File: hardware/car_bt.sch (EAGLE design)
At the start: 51 parts, among them IC2 MIC5209, U1 ATMEGA328P_TQFP, U2 ADP1710-2.5V, Y1 11.0592MHz

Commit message: selected components
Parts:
- added C21: 22uF, resistor:C-EUC1206
- added C22: 22uF, SparkFun-Passives:CAP_POL3528
- C1, C2, C3: value 47uF -> 22uF; device resistor:C-EUC1210 -> resistor:C-EUC1206
- C11, C12, C13, C15, C16, C17, C18, C19, C20, C7, C8: device resistor:C-EUC1210 -> resistor:C-EUC0805
- C4, C5: device resistor:C-EUC0603 -> resistor:C-EUC0805
- L1: value 12uH -> 10uH; device resistor:L-EUL3225P -> resistor:L-EUL3216C
- R1, R11, R12, R13, R14, R2, R21, R3, R4, R5, R6, R7, R8: device rcl:R-EU_R0603 -> rcl:R-EU_R0805
- R10: value 330 -> 360; device rcl:R-EU_R0603 -> rcl:R-EU_R0805
- R9: value 470 -> 360; device rcl:R-EU_R0603 -> rcl:R-EU_R0805
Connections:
- net +5V: now also C2.1, C22.+; no longer C1.1
- net DGND: now also C1.2, C21.2; no longer C2.2
- net GND: now also C2.2, C22.-; no longer C1.2
- net V+: now also C21.1
- net VCC-ISO: now also C1.1; no longer C2.1
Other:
- moved on the sheet: C1, C2

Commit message: v 1.0 of hardware completed
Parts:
- JP2: value (none) -> CAR_IN; device pinhead:PINHD-1X8 -> pinhead:PINHD-1X8/90
- Q2: value (none) -> 2N3904
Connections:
- net V+: no longer R5.1
- net VCC-ISO: now also R5.1
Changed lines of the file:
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@@
 <part name="P+1" library="supply1" deviceset="+5V" device=""/>
 <part name="P+2" library="supply1" deviceset="+5V" device=""/>
-<part name="JP2" library="pinhead" deviceset="PINHD-1X8" device=""/>
+<part name="JP2" library="pinhead" deviceset="PINHD-1X8" device="/90" value="CAR_IN"/>
 <part name="R2" library="rcl" deviceset="R-EU_" device="R0805" value="470"/>
 <part name="R3" library="rcl" deviceset="R-EU_" device="R0805" value="220"/>
@@
 <part name="JP4" library="SparkFun-Connectors" deviceset="M02" device="POLAR_LOCK" value="MIC"/>
 <part name="R5" library="rcl" deviceset="R-EU_" device="R0805" value="220"/>
-<part name="P+8" library="supply1" deviceset="V+" device=""/>
 <part name="SUPPLY3" library="supply2" deviceset="DGND" device=""/>
 <part name="JP5" library="SparkFun-Connectors" deviceset="M01" device="PTH_LONGPAD" value="REMOTE"/>
@@
 <part name="SUPPLY6" library="SparkFun-Aesthetics" deviceset="VCCIO" device=""/>
 <part name="SUPPLY9" library="supply2" deviceset="DGND" device=""/>
-<part name="Q2" library="SparkFun-DiscreteSemi" deviceset="TRANSISTOR_NPN" device="BC547"/>
+<part name="Q2" library="SparkFun-DiscreteSemi" deviceset="TRANSISTOR_NPN" device="BC547" value="2N3904"/>
 <part name="R12" library="rcl" deviceset="R-EU_" device="R0805" value="470"/>
 <part name="SUPPLY10" library="supply2" deviceset="DGND" device=""/>
@@
 <part name="P+18" library="supply1" deviceset="+5V" device=""/>
 <part name="GND15" library="supply1" deviceset="GND" device=""/>
+<part name="U$4" library="SparkFun-Aesthetics" deviceset="VCC-ISO" device=""/>
 </parts>
 <sheets>
@@
 <instance part="JP4" gate="G$1" x="-111.76" y="-96.52"/>
 <instance part="R5" gate="G$1" x="22.86" y="58.42" rot="R270"/>
-<instance part="P+8" gate="1" x="22.86" y="66.04"/>
 <instance part="SUPPLY3" gate="G$1" x="22.86" y="50.8"/>
 <instance part="JP5" gate="G$1" x="30.48" y="2.54" rot="R180"/>
@@
 <instance part="P+18" gate="1" x="-76.2" y="88.9"/>
 <instance part="GND15" gate="1" x="-76.2" y="73.66"/>
+<instance part="U$4" gate="G$1" x="22.86" y="63.5"/>
 </instances>
 <busses>
@@
 <pinref part="C10" gate="G$1" pin="+"/>
 <junction x="-12.7" y="60.96"/>
-</segment>
-<segment>
-<pinref part="R5" gate="G$1" pin="1"/>
-<pinref part="P+8" gate="1" pin="V+"/>
 </segment>
 <segment>
@@
 <net name="N$12" class="1">
 <segment>
-<wire x1="-22.86" y1="-109.22" x2="-25.4" y2="-109.22" width="0.1524" layer="91"/>
-<pinref part="U$1" gate="G$1" pin="RST"/>
-<wire x1="-25.4" y1="-109.22" x2="-30.48" y2="-109.22" width="0.1524" layer="91"/>
-<wire x1="-22.86" y1="-109.22" x2="-25.4" y2="-109.22" width="0.1524" layer="91"/>
 <pinref part="OK4" gate="A" pin="COL"/>
 <wire x1="27.94" y1="-111.76" x2="10.16" y2="-111.76" width="0.1524" layer="91"/>
-<wire x1="10.16" y1="-111.76" x2="-22.86" y2="-111.76" width="0.1524" layer="91"/>
-<wire x1="-22.86" y1="-111.76" x2="-22.86" y2="-109.22" width="0.1524" layer="91"/>
+<wire x1="10.16" y1="-111.76" x2="-25.4" y2="-111.76" width="0.1524" layer="91"/>
 <pinref part="R21" gate="G$1" pin="1"/>
 <junction x="10.16" y="-111.76"/>
 <pinref part="C13" gate="G$1" pin="1"/>
-<wire x1="-22.86" y1="-109.22" x2="-25.4" y2="-109.22" width="0.1524" layer="91"/>
+<wire x1="-25.4" y1="-111.76" x2="-25.4" y2="-109.22" width="0.1524" layer="91"/>
+<pinref part="U$1" gate="G$1" pin="RST"/>
+<wire x1="-25.4" y1="-109.22" x2="-30.48" y2="-109.22" width="0.1524" layer="91"/>
 </segment>
 </net>
@@
 <wire x1="5.08" y1="-58.42" x2="5.08" y2="-60.96" width="0.1524" layer="91"/>
 </segment>
-</net>
+<segment>
+<pinref part="R5" gate="G$1" pin="1"/>
+<pinref part="U$4" gate="G$1" pin="VCC-ISO"/>
+</segment>
+</net>

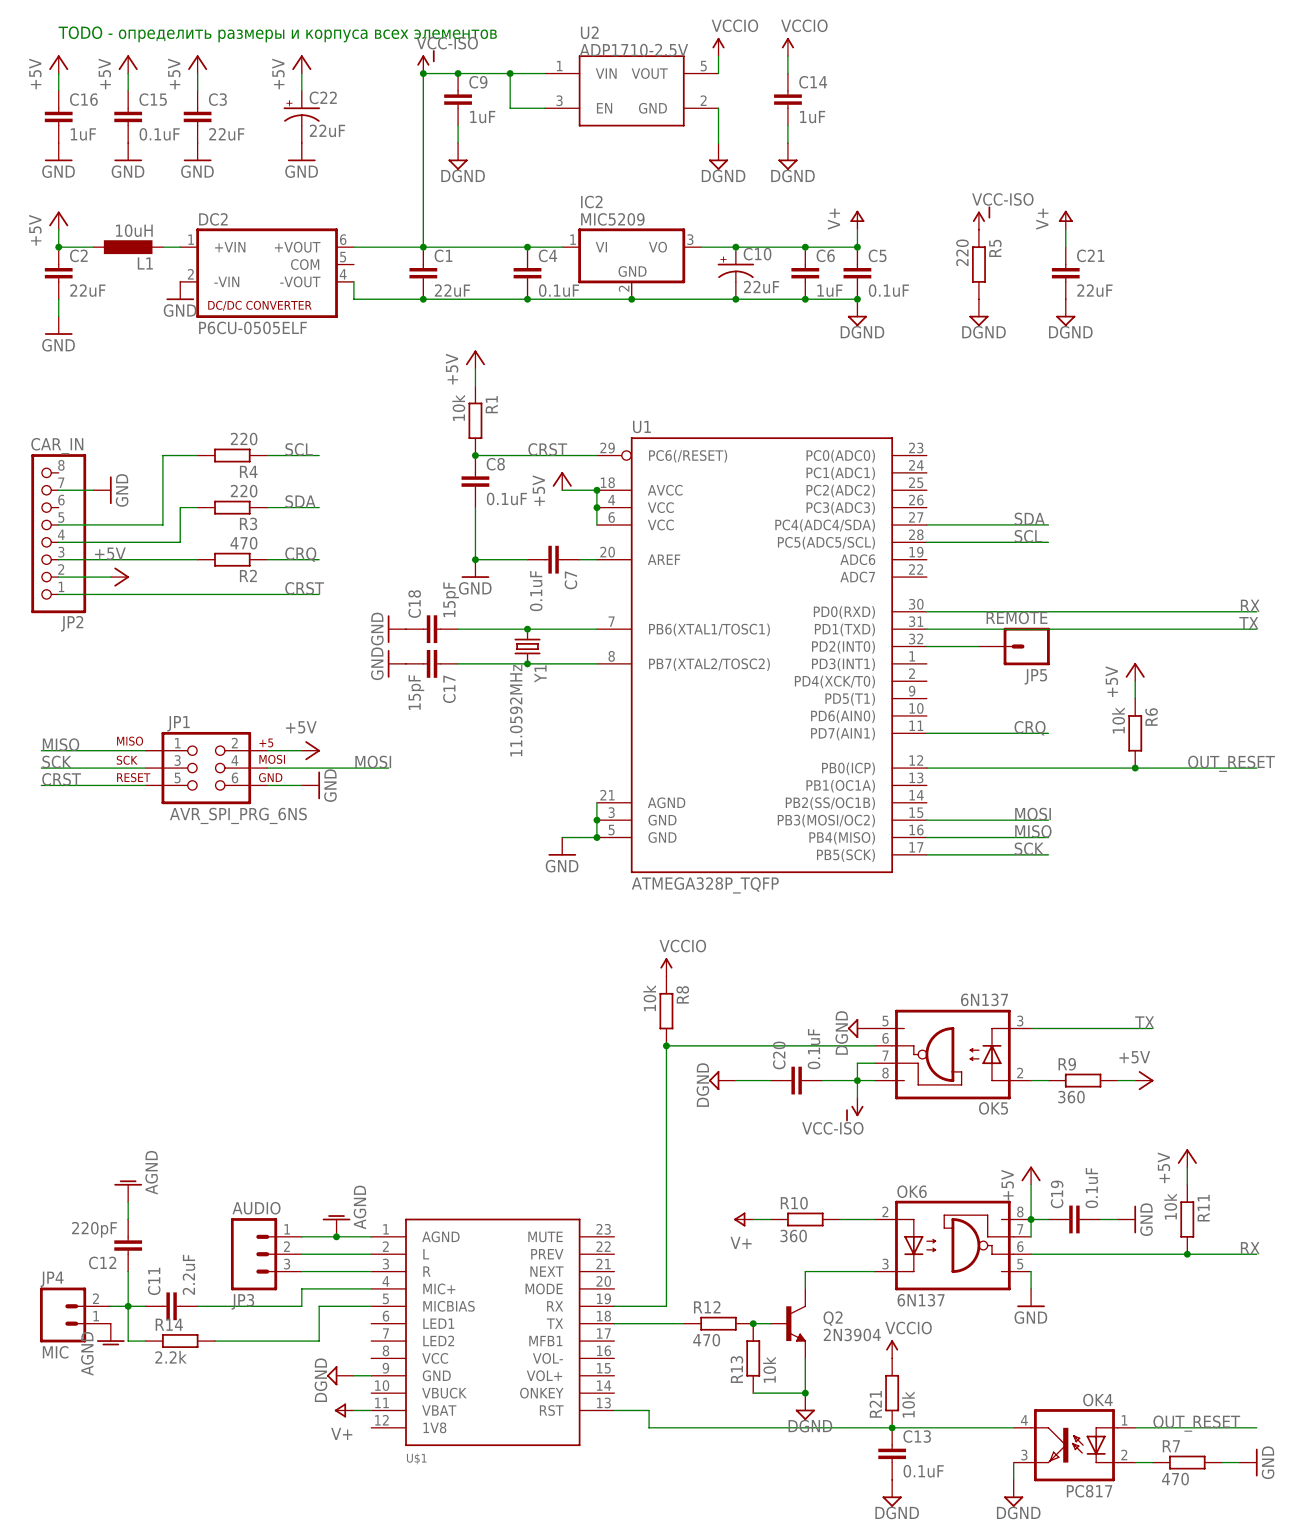
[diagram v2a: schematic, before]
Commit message: switched to uart
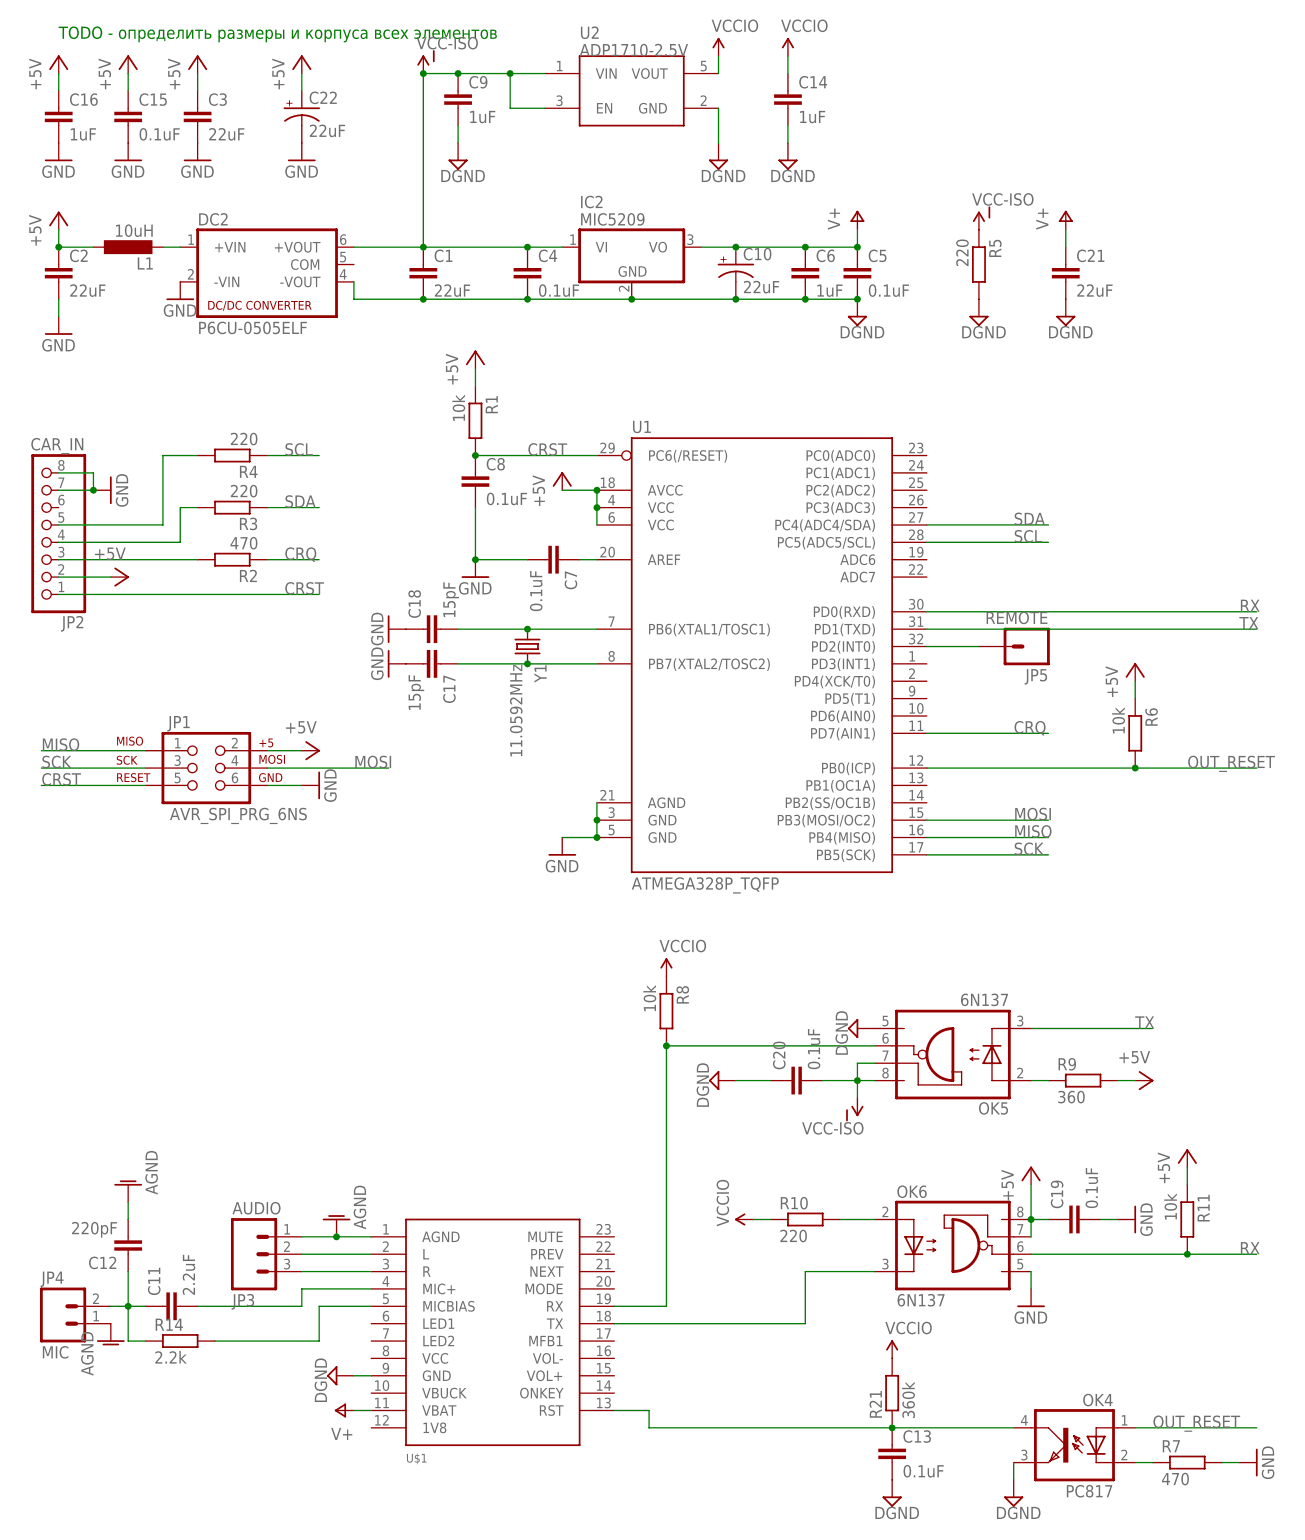
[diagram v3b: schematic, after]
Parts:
- removed Q2: 2N3904, SparkFun-DiscreteSemi:TRANSISTOR_NPNBC547
- removed R12: 470, rcl:R-EU_R0805
- removed R13: 10k, rcl:R-EU_R0805
- R10: value 360 -> 220; device rcl:R-EU_R0805 -> rcl:R-EU_R1206
- R21: value 10k -> 360k
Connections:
- removed net N$17: Q2.B, R12.2, R13.2
- removed net N$21: OK6.C, Q2.C
- net DGND: no longer Q2.E, R13.1
- net GND: now also JP2.8
- net N$5: now also OK6.C; no longer R12.1
- net V+: no longer R10.1
- net VCCIO: now also R10.1
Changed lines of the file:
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@@
 <part name="R14" library="rcl" deviceset="R-EU_" device="R0805" value="2.2k"/>
 <part name="AGND3" library="supply1" deviceset="AGND" device=""/>
-<part name="R21" library="rcl" deviceset="R-EU_" device="R0805" value="10k"/>
+<part name="R21" library="rcl" deviceset="R-EU_" device="R0805" value="360k"/>
 <part name="C13" library="resistor" deviceset="C-EU" device="C0805" value="0.1uF"/>
 <part name="SUPPLY16" library="supply2" deviceset="DGND" device=""/>
@@
 <part name="P+13" library="supply1" deviceset="+5V" device=""/>
 <part name="U$2" library="SparkFun-Aesthetics" deviceset="VCC-ISO" device=""/>
-<part name="R10" library="rcl" deviceset="R-EU_" device="R0805" value="360"/>
-<part name="P+14" library="supply1" deviceset="V+" device=""/>
+<part name="R10" library="rcl" deviceset="R-EU_" device="R1206" value="220"/>
 <part name="Y1" library="SparkFun-FreqCtrl" deviceset="CRYSTAL" device="HC49UV" value="11.0592MHz"/>
 <part name="C17" library="resistor" deviceset="C-EU" device="C0805" value="15pF"/>
@@
 <part name="SUPPLY6" library="SparkFun-Aesthetics" deviceset="VCCIO" device=""/>
 <part name="SUPPLY9" library="supply2" deviceset="DGND" device=""/>
-<part name="Q2" library="SparkFun-DiscreteSemi" deviceset="TRANSISTOR_NPN" device="BC547" value="2N3904"/>
-<part name="R12" library="rcl" deviceset="R-EU_" device="R0805" value="470"/>
-<part name="SUPPLY10" library="supply2" deviceset="DGND" device=""/>
-<part name="R13" library="rcl" deviceset="R-EU_" device="R0805" value="10k"/>
 <part name="C21" library="resistor" deviceset="C-EU" device="C1206" value="22uF"/>
 <part name="P+17" library="supply1" deviceset="V+" device=""/>
@@
 <part name="GND15" library="supply1" deviceset="GND" device=""/>
 <part name="U$4" library="SparkFun-Aesthetics" deviceset="VCC-ISO" device=""/>
+<part name="SUPPLY10" library="SparkFun-Aesthetics" deviceset="VCCIO" device=""/>
 </parts>
 <sheets>
@@
 <instance part="U$2" gate="G$1" x="-58.42" y="86.36"/>
 <instance part="R10" gate="G$1" x="-2.54" y="-81.28"/>
-<instance part="P+14" gate="1" x="-12.7" y="-81.28" rot="R90"/>
 <instance part="Y1" gate="G$1" x="-43.18" y="2.54" rot="R270"/>
 <instance part="C17" gate="G$1" x="-55.88" y="0" rot="R270"/>
@@
 <instance part="SUPPLY6" gate="G$1" x="-22.86" y="-45.72"/>
 <instance part="SUPPLY9" gate="G$1" x="-15.24" y="-60.96" rot="R270"/>
-<instance part="Q2" gate="G$1" x="-5.08" y="-96.52"/>
-<instance part="R12" gate="G$1" x="-15.24" y="-96.52"/>
-<instance part="SUPPLY10" gate="G$1" x="-2.54" y="-109.22"/>
-<instance part="R13" gate="G$1" x="-10.16" y="-101.6" rot="R90"/>
 <instance part="C21" gate="G$1" x="35.56" y="58.42"/>
 <instance part="P+17" gate="1" x="35.56" y="66.04"/>
@@
 <instance part="GND15" gate="1" x="-76.2" y="73.66"/>
 <instance part="U$4" gate="G$1" x="22.86" y="63.5"/>
+<instance part="SUPPLY10" gate="G$1" x="-10.16" y="-81.28" rot="R90"/>
 </instances>
 <busses>
@@
 <wire x1="-106.68" y1="25.4" x2="-111.76" y2="25.4" width="0.1524" layer="91"/>
 <pinref part="JP2" gate="A" pin="7"/>
+<pinref part="JP2" gate="A" pin="8"/>
+<wire x1="-111.76" y1="27.94" x2="-106.68" y2="27.94" width="0.1524" layer="91"/>
+<wire x1="-106.68" y1="27.94" x2="-106.68" y2="25.4" width="0.1524" layer="91"/>
+<junction x="-106.68" y="25.4"/>
 </segment>
 <segment>
@@
 <pinref part="P+5" gate="1" pin="V+"/>
 <wire x1="-68.58" y1="-109.22" x2="-66.04" y2="-109.22" width="0.1524" layer="91"/>
-</segment>
-<segment>
-<pinref part="R10" gate="G$1" pin="1"/>
-<wire x1="-7.62" y1="-81.28" x2="-10.16" y2="-81.28" width="0.1524" layer="91"/>
-<pinref part="P+14" gate="1" pin="V+"/>
 </segment>
 <segment>
@@
 </segment>
 <segment>
-<pinref part="Q2" gate="G$1" pin="E"/>
-<pinref part="SUPPLY10" gate="G$1" pin="DGND"/>
-<wire x1="-2.54" y1="-101.6" x2="-2.54" y2="-106.68" width="0.1524" layer="91"/>
-<pinref part="R13" gate="G$1" pin="1"/>
-<wire x1="-10.16" y1="-106.68" x2="-2.54" y2="-106.68" width="0.1524" layer="91"/>
-<junction x="-2.54" y="-106.68"/>
-</segment>
-<segment>
 <pinref part="C21" gate="G$1" pin="2"/>
 <pinref part="SUPPLY11" gate="G$1" pin="DGND"/>
@@
 <pinref part="R8" gate="G$1" pin="1"/>
 <pinref part="SUPPLY6" gate="G$1" pin="VCCIO"/>
+</segment>
+<segment>
+<pinref part="R10" gate="G$1" pin="1"/>
+<wire x1="-7.62" y1="-81.28" x2="-10.16" y2="-81.28" width="0.1524" layer="91"/>
+<pinref part="SUPPLY10" gate="G$1" pin="VCCIO"/>
 </segment>
 </net>
@@
 </segment>
 </net>
-<net name="N$5" class="1">
-<segment>
-<pinref part="U$1" gate="G$1" pin="TX"/>
-<wire x1="-20.32" y1="-96.52" x2="-30.48" y2="-96.52" width="0.1524" layer="91"/>
-<pinref part="R12" gate="G$1" pin="1"/>
-</segment>
-</net>
 <net name="N$14" class="1">
 <segment>
@@
 </segment>
 </net>
-<net name="N$17" class="1">
-<segment>
-<pinref part="Q2" gate="G$1" pin="B"/>
-<pinref part="R12" gate="G$1" pin="2"/>
-<wire x1="-7.62" y1="-96.52" x2="-10.16" y2="-96.52" width="0.1524" layer="91"/>
-<pinref part="R13" gate="G$1" pin="2"/>
-<junction x="-10.16" y="-96.52"/>
-</segment>
-</net>
-<net name="N$21" class="1">
-<segment>
+<net name="N$5" class="0">
+<segment>
+<pinref part="U$1" gate="G$1" pin="TX"/>
+<wire x1="-30.48" y1="-96.52" x2="-2.54" y2="-96.52" width="0.1524" layer="91"/>
+<wire x1="-2.54" y1="-96.52" x2="-2.54" y2="-88.9" width="0.1524" layer="91"/>
 <pinref part="OK6" gate="A" pin="C"/>
-<pinref part="Q2" gate="G$1" pin="C"/>
-<wire x1="7.62" y1="-88.9" x2="-2.54" y2="-88.9" width="0.1524" layer="91"/>
-<wire x1="-2.54" y1="-88.9" x2="-2.54" y2="-91.44" width="0.1524" layer="91"/>
-</segment>
-</net>
+<wire x1="-2.54" y1="-88.9" x2="7.62" y2="-88.9" width="0.1524" layer="91"/>
+</segment>
+</net>
